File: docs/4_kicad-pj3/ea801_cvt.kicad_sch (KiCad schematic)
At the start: 6 parts, among them J2_BitDogLab Conn_01x06_MountingPin, J2_BitDogLab1 J2_IDC_BitDogLab, M1 Motor principal, M2 Motor Fuso Câmbio, U1 L293D

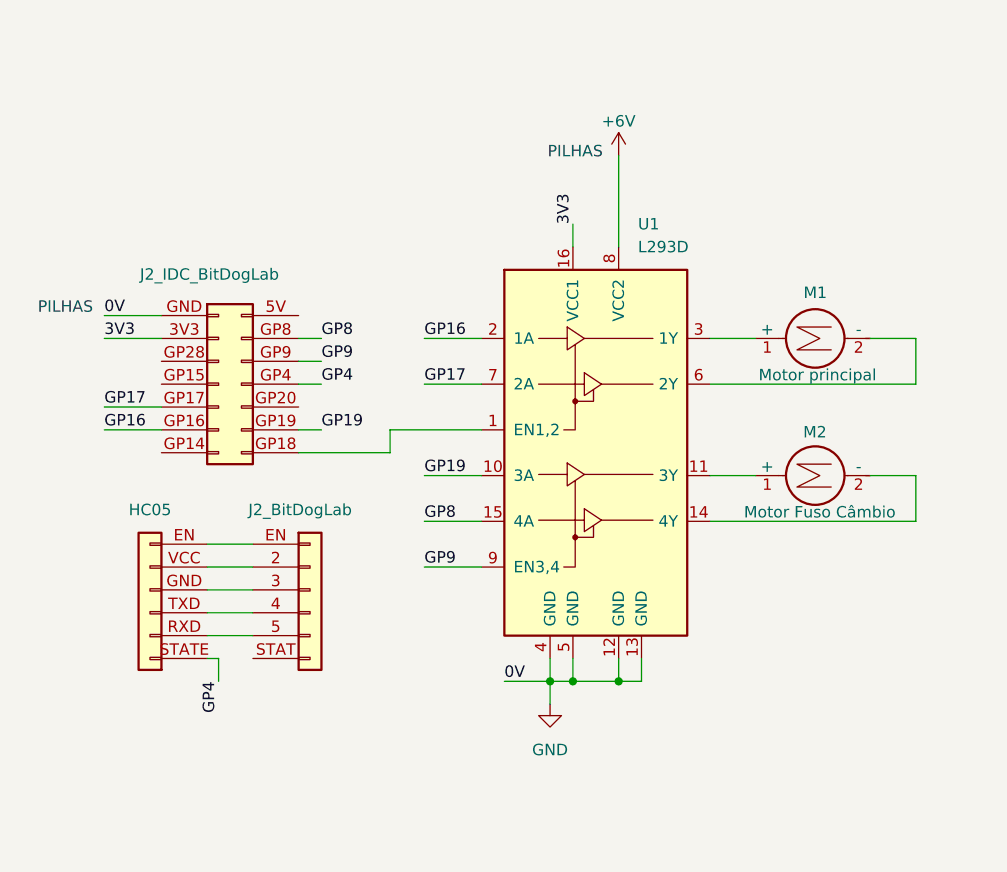
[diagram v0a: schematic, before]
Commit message: datasheet do ToF e testes
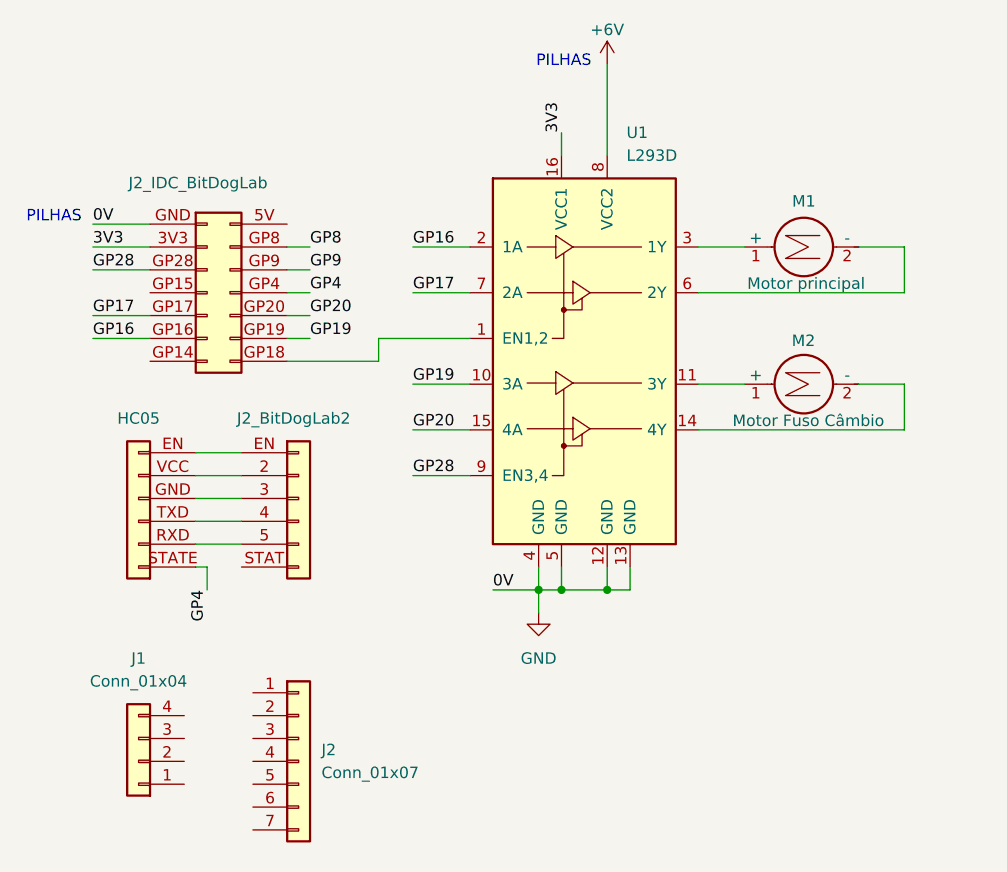
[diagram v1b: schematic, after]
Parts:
- added J1: Conn_01x04, symbol Connector_Generic:Conn_01x04
- added J2: Conn_01x07, symbol Connector_Generic:Conn_01x07
- renumbered J2_BitDogLab to J2_BitDogLab2
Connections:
- net GP8: no longer U1.15 (4A)
- net GP9: no longer U1.9 (EN3,4)
- net GP20: now reaches J2_BitDogLab1.GP20 (Pin_10)
- net GP20: now also U1.15 (4A)
- net GP28: now reaches J2_BitDogLab1.GP28 (Pin_3)
- net GP28: now also U1.9 (EN3,4)
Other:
- moved on the sheet: HC05, J2_BitDogLab2, M1, M2, U1

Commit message: inc imagens, att projeto kicad e att dos arquivos do sensor ToF
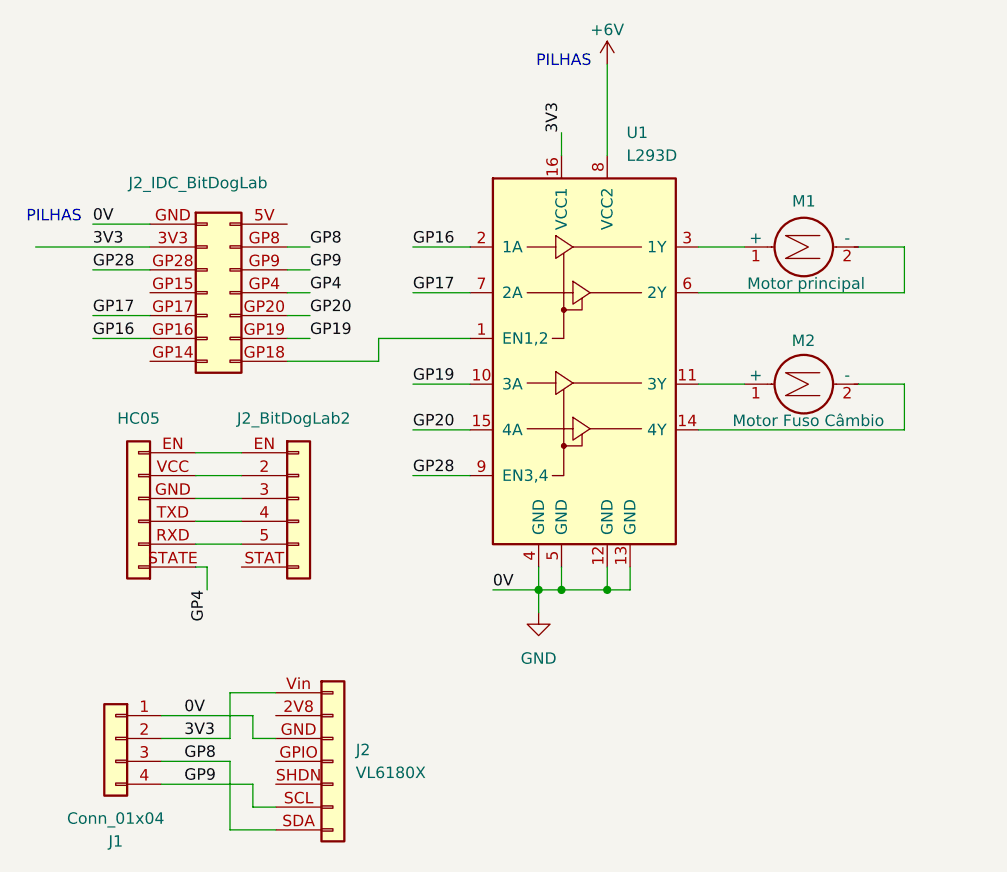
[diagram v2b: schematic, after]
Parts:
- removed J2: Conn_01x07, symbol Connector_Generic:Conn_01x07
- added J2: VL6180X, symbol kicad_tancrer:VL6180X
- J1: footprint (none) -> Connector_PinSocket_2.54mm:PinSocket_1x04_P2.54mm_Vertical
- J2_BitDogLab1: footprint (none) -> Connector_PinSocket_2.54mm:PinSocket_2x07_P2.54mm_Vertical
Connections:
- net 3V3: now also J1.2 (Pin_2), J2.Vin (Pin_1)
- net GND: now also J1.1 (Pin_1), J2.GND (Pin_3)
- net GP8: now also J1.3 (Pin_3), J2.SDA (Pin_7)
- net GP9: now also J1.4 (Pin_4), J2.SCL (Pin_6)
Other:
- moved on the sheet: J1
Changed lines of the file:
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@@
+	(wire
+		(pts
+			(xy 167.64 118.11) (xy 167.64 120.65)
+		)
+		(stroke
+			(width 0)
+			(type default)
+		)
+	)
 	(wire
 		(pts
@@
 	(wire
 		(pts
+			(xy 167.64 125.73) (xy 167.64 128.27)
+		)
+		(stroke
+			(width 0)
+			(type default)
+		)
+	)
+	(wire
+		(pts
 			(xy 201.93 104.14) (xy 207.01 104.14)
 		)
@@
 	(wire
 		(pts
+			(xy 165.1 123.19) (xy 165.1 130.81)
+		)
+		(stroke
+			(width 0)
+			(type default)
+		)
+	)
+	(wire
+		(pts
 			(xy 207.01 45.72) (xy 207.01 55.88)
 		)
@@
 	(wire
 		(pts
+			(xy 165.1 115.57) (xy 170.18 115.57)
+		)
+		(stroke
+			(width 0)
+			(type default)
+		)
+	)
+	(wire
+		(pts
 			(xy 199.39 104.14) (xy 201.93 104.14)
 		)
@@
 	(wire
 		(pts
+			(xy 167.64 128.27) (xy 170.18 128.27)
+		)
+		(stroke
+			(width 0)
+			(type default)
+		)
+	)
+	(wire
+		(pts
 			(xy 185.42 86.36) (xy 191.77 86.36)
 		)
@@
 	(wire
 		(pts
+			(xy 165.1 115.57) (xy 165.1 120.65)
+		)
+		(stroke
+			(width 0)
+			(type default)
+		)
+	)
+	(wire
+		(pts
 			(xy 161.29 88.9) (xy 166.37 88.9)
 		)
@@
 	(wire
 		(pts
+			(xy 167.64 120.65) (xy 170.18 120.65)
+		)
+		(stroke
+			(width 0)
+			(type default)
+		)
+	)
+	(wire
+		(pts
+			(xy 143.51 66.04) (xy 156.21 66.04)
+		)
+		(stroke
+			(width 0)
+			(type default)
+		)
+	)
+	(wire
+		(pts
+			(xy 157.48 118.11) (xy 167.64 118.11)
+		)
+		(stroke
+			(width 0)
+			(type default)
+		)
+	)
+	(wire
+		(pts
 			(xy 185.42 91.44) (xy 191.77 91.44)
 		)
@@
 	(wire
 		(pts
-			(xy 149.86 66.04) (xy 156.21 66.04)
+			(xy 165.1 130.81) (xy 170.18 130.81)
 		)
 		(stroke
@@
 	(wire
 		(pts
+			(xy 157.48 123.19) (xy 165.1 123.19)
+		)
+		(stroke
+			(width 0)
+			(type default)
+		)
+	)
+	(wire
+		(pts
 			(xy 234.95 66.04) (xy 240.03 66.04)
 		)
@@
 	(wire
 		(pts
+			(xy 157.48 125.73) (xy 167.64 125.73)
+		)
+		(stroke
+			(width 0)
+			(type default)
+		)
+	)
+	(wire
+		(pts
 			(xy 171.45 73.66) (xy 173.99 73.66)
+		)
+		(stroke
+			(width 0)
+			(type default)
+		)
+	)
+	(wire
+		(pts
+			(xy 157.48 120.65) (xy 165.1 120.65)
 		)
 		(stroke
@@
 		)
 	)
+	(label "GP8"
+		(at 160.02 123.19 0)
+		(effects
+			(font
+				(size 1.27 1.27)
+			)
+			(justify left bottom)
+		)
+	)
 	(label "GP4"
 		(at 162.56 104.14 270)
@@
 		)
 	)
+	(label "0V"
+		(at 160.02 118.11 0)
+		(effects
+			(font
+				(size 1.27 1.27)
+			)
+			(justify left bottom)
+		)
+	)
 	(label "GP9"
 		(at 173.99 68.58 0)
@@
 		)
 	)
+	(label "GP9"
+		(at 160.02 125.73 0)
+		(effects
+			(font
+				(size 1.27 1.27)
+			)
+			(justify left bottom)
+		)
+	)
 	(label "GP19"
 		(at 173.99 76.2 0)
@@
 	)
 	(label "3V3"
+		(at 160.02 120.65 0)
+		(effects
+			(font
+				(size 1.27 1.27)
+			)
+			(justify left bottom)
+		)
+	)
+	(label "3V3"
 		(at 149.86 66.04 0)
 		(effects
@@
 			)
 			(justify left bottom)
-		)
-	)
-	(symbol
-		(lib_id "Connector_Generic:Conn_01x07")
-		(at 172.72 123.19 0)
-		(unit 1)
-		(body_style 1)
-		(exclude_from_sim no)
-		(in_bom yes)
-		(on_board yes)
-		(in_pos_files yes)
-		(dnp no)
-		(fields_autoplaced yes)
-		(property "Reference" "J2"
-			(at 175.26 121.9199 0)
-			(show_name no)
-			(do_not_autoplace no)
-			(effects
-				(font
-					(size 1.27 1.27)
-				)
-				(justify left)
-			)
-		)
-		(property "Value" "Conn_01x07"
-			(at 175.26 124.4599 0)
-			(show_name no)
-			(do_not_autoplace no)
-			(effects
-				(font
-					(size 1.27 1.27)
-				)
-				(justify left)
-			)
-		)
-		(property "Footprint" ""
-			(at 172.72 123.19 0)
-			(hide yes)
-			(show_name no)
-			(do_not_autoplace no)
-			(effects
-				(font
-					(size 1.27 1.27)
-				)
-			)
-		)
-		(property "Datasheet" ""
-			(at 172.72 123.19 0)
-			(hide yes)
-			(show_name no)
-			(do_not_autoplace no)
-			(effects
-				(font
-					(size 1.27 1.27)
-				)
-			)
-		)
-		(property "Description" "Generic connector, single row, 01x07, script generated (kicad-library-utils/schlib/autogen/connector/)"
-			(at 172.72 123.19 0)
-			(hide yes)
-			(show_name no)
-			(do_not_autoplace no)
-			(effects
-				(font
-					(size 1.27 1.27)
-				)
-			)
-		)
-		(pin "4"
-		)
-		(pin "3"
-		)
-		(pin "6"
-		)
-		(pin "7"
-		)
-		(pin "1"
-		)
-		(pin "5"
-		)
-		(pin "2"
-		)
-		(instances
-			(project "ea801_cvt"
-				(path "/0e0d7852-58b0-4957-a97f-76f6ac234760"
-					(reference "J2")
-					(unit 1)
-				)
-			)
 		)
 	)
@@
 	(symbol
 		(lib_id "Connector_Generic:Conn_01x04")
-		(at 154.94 123.19 180)
+		(at 152.4 120.65 0)
+		(mirror y)
 		(unit 1)
 		(body_style 1)
@@
 		(in_pos_files yes)
 		(dnp no)
-		(fields_autoplaced yes)
 		(property "Reference" "J1"
-			(at 154.94 111.76 0)
+			(at 152.4 132.08 0)
 			(show_name no)
 			(do_not_autoplace no)
@@
 		)
 		(property "Value" "Conn_01x04"
-			(at 154.94 114.3 0)
-			(show_name no)
-			(do_not_autoplace no)
-			(effects
-				(font
-					(size 1.27 1.27)
-				)
-			)
-		)
-		(property "Footprint" ""
-			(at 154.94 123.19 0)
+			(at 152.4 129.54 0)
+			(show_name no)
+			(do_not_autoplace no)
+			(effects
+				(font
+					(size 1.27 1.27)
+				)
+			)
+		)
+		(property "Footprint" "Connector_PinSocket_2.54mm:PinSocket_1x04_P2.54mm_Vertical"
+			(at 152.4 120.65 0)
 			(hide yes)
 			(show_name no)
@@
 		)
 		(property "Datasheet" ""
-			(at 154.94 123.19 0)
+			(at 152.4 120.65 0)
 			(hide yes)
 			(show_name no)
@@
 		)
 		(property "Description" "Generic connector, single row, 01x04, script generated (kicad-library-utils/schlib/autogen/connector/)"
-			(at 154.94 123.19 0)
+			(at 152.4 120.65 0)
 			(hide yes)
 			(show_name no)
@@
 	)
 	(symbol
+		(lib_id "kicad_tancrer:VL6180X")
+		(at 176.53 123.19 0)
+		(unit 1)
+		(body_style 1)
+		(exclude_from_sim no)
+		(in_bom yes)
+		(on_board yes)
+		(in_pos_files yes)
+		(dnp no)
+		(fields_autoplaced yes)
+		(property "Reference" "J2"
+			(at 179.07 121.9199 0)
+			(show_name no)
+			(do_not_autoplace no)
+			(effects
+				(font
+					(size 1.27 1.27)
+				)
+				(justify left)
+			)
+		)
+		(property "Value" "VL6180X"
+			(at 179.07 124.4599 0)
+			(show_name no)
+			(do_not_autoplace no)
+			(effects
+				(font
+					(size 1.27 1.27)
+				)
+				(justify left)
+			)
+		)
+		(property "Footprint" ""
+			(at 176.53 123.19 0)
+			(hide yes)
+			(show_name no)
+			(do_not_autoplace no)
+			(effects
+				(font
+					(size 1.27 1.27)
+				)
+			)
+		)
+		(property "Datasheet" ""
+			(at 176.53 123.19 0)
+			(hide yes)
+			(show_name no)
+			(do_not_autoplace no)
+			(effects
+				(font
+					(size 1.27 1.27)
+				)
+			)
+		)
+		(property "Description" "Generic connector, single row, 01x07, script generated (kicad-library-utils/schlib/autogen/connector/)"
+			(at 176.53 123.19 0)
+			(hide yes)
+			(show_name no)
+			(do_not_autoplace no)
+			(effects
+				(font
+					(size 1.27 1.27)
+				)
+			)
+		)
+		(pin "SDA"
+		)
+		(pin "2V8"
+		)
+		(pin "GPIO"
+		)
+		(pin "SCL"
+		)
+		(pin "GND"
+		)
+		(pin "Vin"
+		)
+		(pin "SHDN"
+		)
+		(instances
+			(project "ea801_cvt"
+				(path "/0e0d7852-58b0-4957-a97f-76f6ac234760"
+					(reference "J2")
+					(unit 1)
+				)
+			)
+		)
+	)
+	(symbol
 		(lib_id "Motor:Motor_DC")
 		(at 227.33 81.28 90)
@@
 			)
 		)
-		(property "Footprint" ""
+		(property "Footprint" "Connector_PinSocket_2.54mm:PinSocket_2x07_P2.54mm_Vertical"
 			(at 162.56 71.12 0)
 			(hide yes)

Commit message: asbuilt do projeto do schematic
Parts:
- added C1, C2: 100n, symbol Device:C
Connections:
- net at M2.1 (+), U1.11 (3Y): now also C2.1
- net at M2.2 (-), U1.14 (4Y): now also C2.2
- net at M1.1 (+), U1.3 (1Y): now also C1.1
- net at M1.2 (-), U1.6 (2Y): now also C1.2
- net +6V renamed +3.7V
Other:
- note added: "2x 18650"
- note removed: "PILHAS"
- moved on the sheet: HC05, J1, J2, J2_BitDogLab2, M1, M2
